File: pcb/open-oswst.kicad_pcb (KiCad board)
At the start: 2 copper layers, 70 x 50 mm, 14 parts

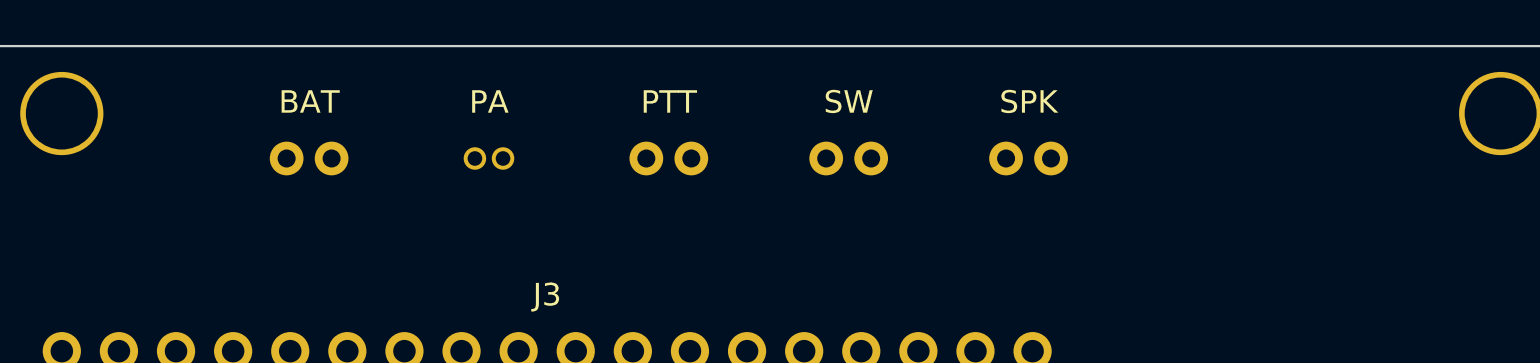
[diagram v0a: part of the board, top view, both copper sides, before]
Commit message: Add rotary encoder connectors to PCB
Two 4-pin JST-PH connectors (ENC1, ENC2) for EC11 rotary encoders
with push buttons (A, B, SW, GND). Wired to GPIO 1/2/6 and 33/47/48.
Rebalanced top-edge connector spacing to fit all 7 connectors.

Co-Authored-By: Claude Opus 4.6 <noreply@anthropic.com>
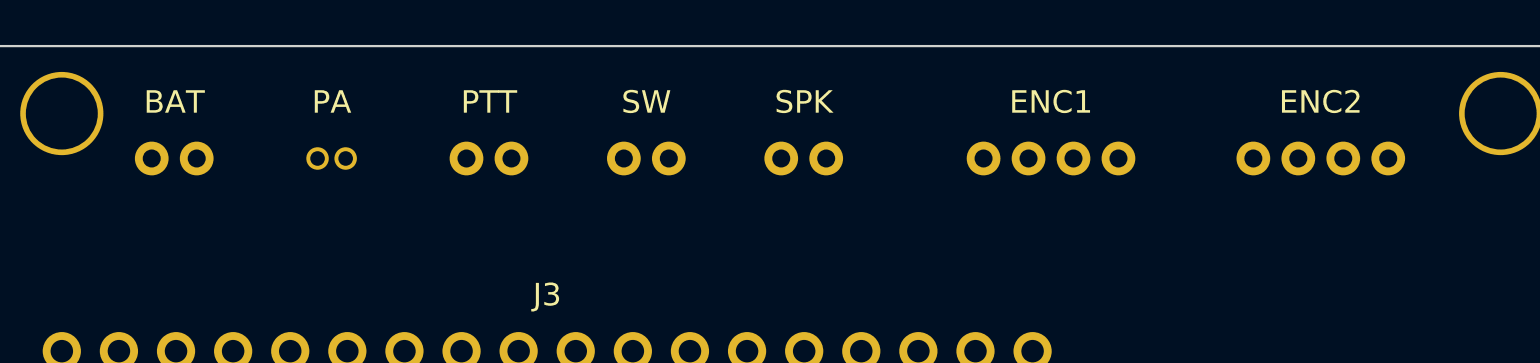
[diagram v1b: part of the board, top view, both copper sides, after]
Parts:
- added ENC1: , JST_PH_B4B, F.Cu at (160.0, 118.0)
- added ENC2: , JST_PH_B4B, F.Cu at (172.0, 118.0)
- moved SPK 10.0 mm to (149.0, 118.0)
- moved SW 9.00 mm to (142.0, 118.0)
- moved PTT 8.00 mm to (135.0, 118.0)
- moved PA 7.00 mm to (128.0, 118.0)
- moved BAT 6.00 mm to (121.0, 118.0)
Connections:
- J2 pad GPIO33: (no net) -> ENC2_A
- J2 pad GPIO47: (no net) -> ENC2_B
- J2 pad GPIO48: (no net) -> ENC2_SW
- J3 pad GPIO1: (no net) -> ENC1_A
- J3 pad GPIO2: (no net) -> ENC1_B
- J3 pad GPIO6: (no net) -> ENC1_SW
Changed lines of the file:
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@@
   (net 5 "SPK+")
   (net 6 "SPK-")
-  (net 7 "3V3")
-  (net 8 "BCLK")
-  (net 9 "LRC")
-  (net 10 "DIN")
-  (net 11 "MIC_OUT")
+  (net 7 "ENC1_A")
+  (net 8 "ENC1_B")
+  (net 9 "ENC1_SW")
+  (net 10 "ENC2_A")
+  (net 11 "ENC2_B")
+  (net 12 "ENC2_SW")
+  (net 13 "3V3")
+  (net 14 "BCLK")
+  (net 15 "LRC")
+  (net 16 "DIN")
+  (net 17 "MIC_OUT")
   (net_class "Default" ""
     (clearance 0.2)
@@
   (footprint "JST_PH_B2B"
     (layer "F.Cu")
-    (at 127 118)
+    (at 121 118)
     (fp_text reference "BAT" (at 0 -2.5) (layer "F.SilkS")
       (effects (font (size 1 1) (thickness 0.15)))
@@
   (footprint "JST_SH_B2B"
     (layer "F.Cu")
-    (at 135 118)
+    (at 128 118)
     (fp_text reference "PA" (at 0 -2.5) (layer "F.SilkS")
       (effects (font (size 1 1) (thickness 0.15)))
@@
   (footprint "JST_PH_B2B"
     (layer "F.Cu")
-    (at 143 118)
+    (at 135 118)
     (fp_text reference "PTT" (at 0 -2.5) (layer "F.SilkS")
       (effects (font (size 1 1) (thickness 0.15)))
@@
   (footprint "JST_PH_B2B"
     (layer "F.Cu")
-    (at 151 118)
+    (at 142 118)
     (fp_text reference "SW" (at 0 -2.5) (layer "F.SilkS")
       (effects (font (size 1 1) (thickness 0.15)))
@@
   (footprint "JST_PH_B2B"
     (layer "F.Cu")
-    (at 159 118)
+    (at 149 118)
     (fp_text reference "SPK" (at 0 -2.5) (layer "F.SilkS")
       (effects (font (size 1 1) (thickness 0.15)))
@@
     )
   )
+  (footprint "JST_PH_B4B"
+    (layer "F.Cu")
+    (at 160 118)
+    (fp_text reference "ENC1" (at 0 -2.5) (layer "F.SilkS")
+      (effects (font (size 1 1) (thickness 0.15)))
+    )
+    (pad "A" thru_hole circle
+      (at -3.0 0)
+      (size 1.5 1.5)
+      (drill 0.8)
+      (layers *.Cu *.Mask)
+      (net 7 "ENC1_A")
+    )
+    (pad "B" thru_hole circle
+      (at -1.0 0)
+      (size 1.5 1.5)
+      (drill 0.8)
+      (layers *.Cu *.Mask)
+      (net 8 "ENC1_B")
+    )
+    (pad "SW" thru_hole circle
+      (at 1.0 0)
+      (size 1.5 1.5)
+      (drill 0.8)
+      (layers *.Cu *.Mask)
+      (net 9 "ENC1_SW")
+    )
+    (pad "GND" thru_hole circle
+      (at 3.0 0)
+      (size 1.5 1.5)
+      (drill 0.8)
+      (layers *.Cu *.Mask)
+      (net 2 "GND")
+    )
+  )
+  (footprint "JST_PH_B4B"
+    (layer "F.Cu")
+    (at 172 118)
+    (fp_text reference "ENC2" (at 0 -2.5) (layer "F.SilkS")
+      (effects (font (size 1 1) (thickness 0.15)))
+    )
+    (pad "A" thru_hole circle
+      (at -3.0 0)
+      (size 1.5 1.5)
+      (drill 0.8)
+      (layers *.Cu *.Mask)
+      (net 10 "ENC2_A")
+    )
+    (pad "B" thru_hole circle
+      (at -1.0 0)
+      (size 1.5 1.5)
+      (drill 0.8)
+      (layers *.Cu *.Mask)
+      (net 11 "ENC2_B")
+    )
+    (pad "SW" thru_hole circle
+      (at 1.0 0)
+      (size 1.5 1.5)
+      (drill 0.8)
+      (layers *.Cu *.Mask)
+      (net 12 "ENC2_SW")
+    )
+    (pad "GND" thru_hole circle
+      (at 3.0 0)
+      (size 1.5 1.5)
+      (drill 0.8)
+      (layers *.Cu *.Mask)
+      (net 2 "GND")
+    )
+  )
   (footprint "PinHeader_1x18_P2.54mm"
     (layer "F.Cu")
@@
       (drill 1.0)
       (layers *.Cu *.Mask)
-      (net 7 "3V3")
+      (net 13 "3V3")
     )
     (pad "GPIO37" thru_hole circle
@@
       (drill 1.0)
       (layers *.Cu *.Mask)
+      (net 7 "ENC1_A")
     )
     (pad "GPIO2" thru_hole circle
@@
       (drill 1.0)
       (layers *.Cu *.Mask)
+      (net 8 "ENC1_B")
     )
     (pad "GPIO3" thru_hole circle
@@
       (drill 1.0)
       (layers *.Cu *.Mask)
-      (net 8 "BCLK")
+      (net 14 "BCLK")
     )
     (pad "GPIO4" thru_hole circle
@@
       (drill 1.0)
       (layers *.Cu *.Mask)
-      (net 9 "LRC")
+      (net 15 "LRC")
     )
     (pad "GPIO5" thru_hole circle
@@
       (drill 1.0)
       (layers *.Cu *.Mask)
-      (net 10 "DIN")
+      (net 16 "DIN")
     )
     (pad "GPIO6" thru_hole circle
@@
       (drill 1.0)
       (layers *.Cu *.Mask)
+      (net 9 "ENC1_SW")
     )
     (pad "GPIO7" thru_hole circle
@@
       (drill 1.0)
       (layers *.Cu *.Mask)
-      (net 11 "MIC_OUT")
+      (net 17 "MIC_OUT")
     )
   )
@@
       (drill 1.0)
       (layers *.Cu *.Mask)
+      (net 10 "ENC2_A")
     )
     (pad "GPIO47" thru_hole circle
@@
       (drill 1.0)
       (layers *.Cu *.Mask)
+      (net 11 "ENC2_B")
     )
     (pad "GPIO48" thru_hole circle
@@
       (drill 1.0)
       (layers *.Cu *.Mask)
+      (net 12 "ENC2_SW")
     )
     (pad "GPIO26" thru_hole circle
@@
       (drill 1.0)
       (layers *.Cu *.Mask)
-      (net 11 "MIC_OUT")
+      (net 17 "MIC_OUT")
     )
     (pad "GND" thru_hole circle
@@
       (drill 1.0)
       (layers *.Cu *.Mask)
-      (net 7 "3V3")
+      (net 13 "3V3")
     )
     (pad "AR" thru_hole circle
@@
       (drill 1.0)
       (layers *.Cu *.Mask)
-      (net 7 "3V3")
+      (net 13 "3V3")
     )
     (pad "GND" thru_hole circle
@@
       (drill 1.0)
       (layers *.Cu *.Mask)
-      (net 10 "DIN")
+      (net 16 "DIN")
     )
     (pad "BCLK" thru_hole circle
@@
       (drill 1.0)
       (layers *.Cu *.Mask)
-      (net 8 "BCLK")
+      (net 14 "BCLK")
     )
     (pad "LRC" thru_hole circle
@@
       (drill 1.0)
       (layers *.Cu *.Mask)
-      (net 9 "LRC")
-    )
-  )
+      (net 15 "LRC")
+    )
+  )

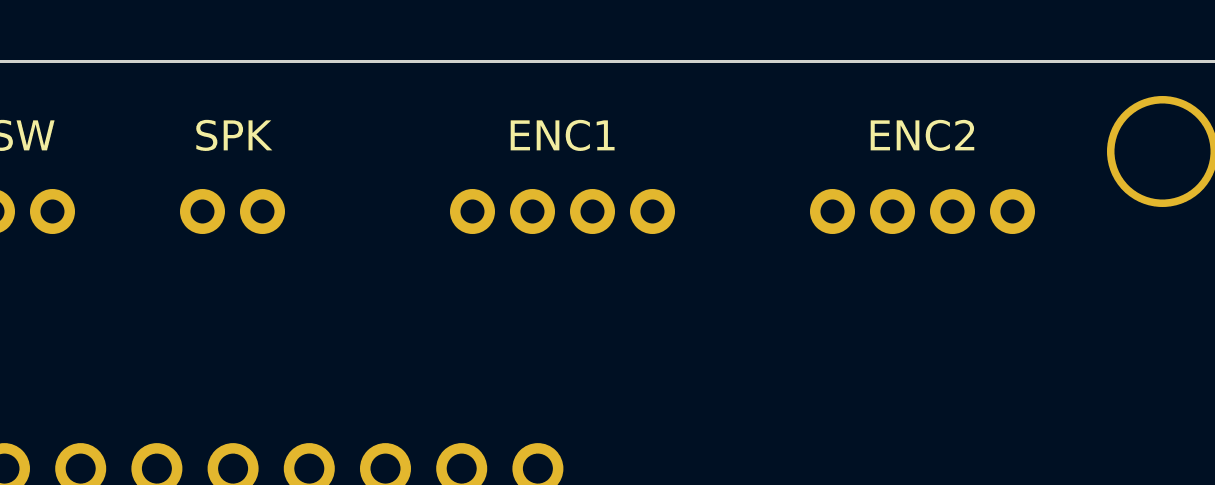
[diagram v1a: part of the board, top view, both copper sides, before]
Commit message: PCB: add encoders, rename labels, optimize GPIO locality
- Rename ENC1→VOL, ENC2→CHNL
- Move SPK to end of top-edge connector row
- Swap I2S (BCLK/LRC/DIN) to J2 GPIO 33/47/48 (near AMP)
- Move CHNL to J3 GPIO 5/6/7 (near top-edge connector)
- Group J3 pins: VOL(1,2,3), MIC(4), CHNL(5,6,7)

Co-Authored-By: Claude Opus 4.6 <noreply@anthropic.com>
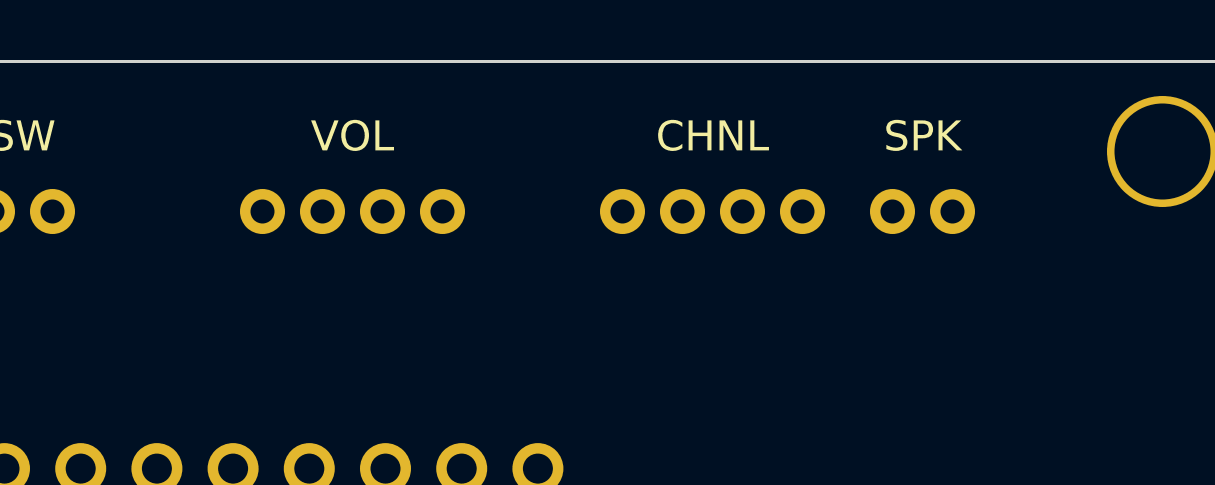
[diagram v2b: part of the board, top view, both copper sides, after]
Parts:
- removed ENC1, ENC2: , JST_PH_B4B
- added CHNL: , JST_PH_B4B, F.Cu at (165.0, 118.0)
- added VOL: , JST_PH_B4B, F.Cu at (153.0, 118.0)
- moved SPK 23.0 mm to (172.0, 118.0)
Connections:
- J2 pad GPIO33: ENC2_A -> BCLK
- J2 pad GPIO47: ENC2_B -> LRC
- J2 pad GPIO48: ENC2_SW -> DIN
- J3 pad GPIO1: ENC1_A -> VOL_A
- J3 pad GPIO2: ENC1_B -> VOL_B
- J3 pad GPIO3: BCLK -> VOL_SW
- J3 pad GPIO4: LRC -> MIC_OUT
- J3 pad GPIO5: DIN -> CHNL_A
- J3 pad GPIO6: ENC1_SW -> CHNL_B
- J3 pad GPIO7: MIC_OUT -> CHNL_SW
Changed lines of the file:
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@@
   (net 3 "VSW")
   (net 4 "PTT")
-  (net 5 "SPK+")
-  (net 6 "SPK-")
-  (net 7 "ENC1_A")
-  (net 8 "ENC1_B")
-  (net 9 "ENC1_SW")
-  (net 10 "ENC2_A")
-  (net 11 "ENC2_B")
-  (net 12 "ENC2_SW")
+  (net 5 "VOL_A")
+  (net 6 "VOL_B")
+  (net 7 "VOL_SW")
+  (net 8 "CHNL_A")
+  (net 9 "CHNL_B")
+  (net 10 "CHNL_SW")
+  (net 11 "SPK+")
+  (net 12 "SPK-")
   (net 13 "3V3")
-  (net 14 "BCLK")
-  (net 15 "LRC")
-  (net 16 "DIN")
-  (net 17 "MIC_OUT")
+  (net 14 "MIC_OUT")
+  (net 15 "BCLK")
+  (net 16 "LRC")
+  (net 17 "DIN")
   (net_class "Default" ""
     (clearance 0.2)
@@
     )
   )
+  (footprint "JST_PH_B4B"
+    (layer "F.Cu")
+    (at 153 118)
+    (fp_text reference "VOL" (at 0 -2.5) (layer "F.SilkS")
+      (effects (font (size 1 1) (thickness 0.15)))
+    )
+    (pad "A" thru_hole circle
+      (at -3.0 0)
+      (size 1.5 1.5)
+      (drill 0.8)
+      (layers *.Cu *.Mask)
+      (net 5 "VOL_A")
+    )
+    (pad "B" thru_hole circle
+      (at -1.0 0)
+      (size 1.5 1.5)
+      (drill 0.8)
+      (layers *.Cu *.Mask)
+      (net 6 "VOL_B")
+    )
+    (pad "SW" thru_hole circle
+      (at 1.0 0)
+      (size 1.5 1.5)
+      (drill 0.8)
+      (layers *.Cu *.Mask)
+      (net 7 "VOL_SW")
+    )
+    (pad "GND" thru_hole circle
+      (at 3.0 0)
+      (size 1.5 1.5)
+      (drill 0.8)
+      (layers *.Cu *.Mask)
+      (net 2 "GND")
+    )
+  )
+  (footprint "JST_PH_B4B"
+    (layer "F.Cu")
+    (at 165 118)
+    (fp_text reference "CHNL" (at 0 -2.5) (layer "F.SilkS")
+      (effects (font (size 1 1) (thickness 0.15)))
+    )
+    (pad "A" thru_hole circle
+      (at -3.0 0)
+      (size 1.5 1.5)
+      (drill 0.8)
+      (layers *.Cu *.Mask)
+      (net 8 "CHNL_A")
+    )
+    (pad "B" thru_hole circle
+      (at -1.0 0)
+      (size 1.5 1.5)
+      (drill 0.8)
+      (layers *.Cu *.Mask)
+      (net 9 "CHNL_B")
+    )
+    (pad "SW" thru_hole circle
+      (at 1.0 0)
+      (size 1.5 1.5)
+      (drill 0.8)
+      (layers *.Cu *.Mask)
+      (net 10 "CHNL_SW")
+    )
+    (pad "GND" thru_hole circle
+      (at 3.0 0)
+      (size 1.5 1.5)
+      (drill 0.8)
+      (layers *.Cu *.Mask)
+      (net 2 "GND")
+    )
+  )
   (footprint "JST_PH_B2B"
     (layer "F.Cu")
-    (at 149 118)
+    (at 172 118)
     (fp_text reference "SPK" (at 0 -2.5) (layer "F.SilkS")
       (effects (font (size 1 1) (thickness 0.15)))
@@
       (drill 0.8)
       (layers *.Cu *.Mask)
-      (net 5 "SPK+")
+      (net 11 "SPK+")
     )
     (pad "-" thru_hole circle
@@
       (drill 0.8)
       (layers *.Cu *.Mask)
-      (net 6 "SPK-")
-    )
-  )
-  (footprint "JST_PH_B4B"
-    (layer "F.Cu")
-    (at 160 118)
-    (fp_text reference "ENC1" (at 0 -2.5) (layer "F.SilkS")
-      (effects (font (size 1 1) (thickness 0.15)))
-    )
-    (pad "A" thru_hole circle
-      (at -3.0 0)
-      (size 1.5 1.5)
-      (drill 0.8)
-      (layers *.Cu *.Mask)
-      (net 7 "ENC1_A")
-    )
-    (pad "B" thru_hole circle
-      (at -1.0 0)
-      (size 1.5 1.5)
-      (drill 0.8)
-      (layers *.Cu *.Mask)
-      (net 8 "ENC1_B")
-    )
-    (pad "SW" thru_hole circle
-      (at 1.0 0)
-      (size 1.5 1.5)
-      (drill 0.8)
-      (layers *.Cu *.Mask)
-      (net 9 "ENC1_SW")
-    )
-    (pad "GND" thru_hole circle
-      (at 3.0 0)
-      (size 1.5 1.5)
-      (drill 0.8)
-      (layers *.Cu *.Mask)
-      (net 2 "GND")
-    )
-  )
-  (footprint "JST_PH_B4B"
-    (layer "F.Cu")
-    (at 172 118)
-    (fp_text reference "ENC2" (at 0 -2.5) (layer "F.SilkS")
-      (effects (font (size 1 1) (thickness 0.15)))
-    )
-    (pad "A" thru_hole circle
-      (at -3.0 0)
-      (size 1.5 1.5)
-      (drill 0.8)
-      (layers *.Cu *.Mask)
-      (net 10 "ENC2_A")
-    )
-    (pad "B" thru_hole circle
-      (at -1.0 0)
-      (size 1.5 1.5)
-      (drill 0.8)
-      (layers *.Cu *.Mask)
-      (net 11 "ENC2_B")
-    )
-    (pad "SW" thru_hole circle
-      (at 1.0 0)
-      (size 1.5 1.5)
-      (drill 0.8)
-      (layers *.Cu *.Mask)
-      (net 12 "ENC2_SW")
-    )
-    (pad "GND" thru_hole circle
-      (at 3.0 0)
-      (size 1.5 1.5)
-      (drill 0.8)
-      (layers *.Cu *.Mask)
-      (net 2 "GND")
+      (net 12 "SPK-")
     )
   )
@@
       (drill 1.0)
       (layers *.Cu *.Mask)
-      (net 7 "ENC1_A")
+      (net 5 "VOL_A")
     )
     (pad "GPIO2" thru_hole circle
@@
       (drill 1.0)
       (layers *.Cu *.Mask)
-      (net 8 "ENC1_B")
+      (net 6 "VOL_B")
     )
     (pad "GPIO3" thru_hole circle
@@
       (drill 1.0)
       (layers *.Cu *.Mask)
-      (net 14 "BCLK")
+      (net 7 "VOL_SW")
     )
     (pad "GPIO4" thru_hole circle
@@
       (drill 1.0)
       (layers *.Cu *.Mask)
-      (net 15 "LRC")
+      (net 14 "MIC_OUT")
     )
     (pad "GPIO5" thru_hole circle
@@
       (drill 1.0)
       (layers *.Cu *.Mask)
-      (net 16 "DIN")
+      (net 8 "CHNL_A")
     )
     (pad "GPIO6" thru_hole circle
@@
       (drill 1.0)
       (layers *.Cu *.Mask)
-      (net 9 "ENC1_SW")
+      (net 9 "CHNL_B")
     )
     (pad "GPIO7" thru_hole circle
@@
       (drill 1.0)
       (layers *.Cu *.Mask)
-      (net 17 "MIC_OUT")
+      (net 10 "CHNL_SW")
     )
   )
@@
       (drill 1.0)
       (layers *.Cu *.Mask)
-      (net 10 "ENC2_A")
+      (net 15 "BCLK")
     )
     (pad "GPIO47" thru_hole circle
@@
       (drill 1.0)
       (layers *.Cu *.Mask)
-      (net 11 "ENC2_B")
+      (net 16 "LRC")
     )
     (pad "GPIO48" thru_hole circle
@@
       (drill 1.0)
       (layers *.Cu *.Mask)
-      (net 12 "ENC2_SW")
+      (net 17 "DIN")
     )
     (pad "GPIO26" thru_hole circle
@@
       (drill 1.0)
       (layers *.Cu *.Mask)
-      (net 17 "MIC_OUT")
+      (net 14 "MIC_OUT")
     )
     (pad "GND" thru_hole circle
@@
       (drill 1.0)
       (layers *.Cu *.Mask)
-      (net 16 "DIN")
+      (net 17 "DIN")
     )
     (pad "BCLK" thru_hole circle
@@
       (drill 1.0)
       (layers *.Cu *.Mask)
-      (net 14 "BCLK")
+      (net 15 "BCLK")
     )
     (pad "LRC" thru_hole circle
@@
       (drill 1.0)
       (layers *.Cu *.Mask)
-      (net 15 "LRC")
+      (net 16 "LRC")
     )
   )
@@
       (drill 1.0)
       (layers *.Cu *.Mask)
-      (net 5 "SPK+")
+      (net 11 "SPK+")
     )
     (pad "-" thru_hole circle
@@
       (drill 1.0)
       (layers *.Cu *.Mask)
-      (net 6 "SPK-")
-    )
-  )
+      (net 12 "SPK-")
+    )
+  )
